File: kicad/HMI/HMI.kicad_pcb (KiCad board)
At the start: 2 copper layers, 47 x 107.1 mm, 57 parts, among them J2 SWD, J3 DEM 128128A TMH-PW-N, J4 RIBBON, SW1 SW_Push, SW10 SW_Push, SW11 SW_Push, SW12 SW_Push, SW13 SW_Push, SW14 SW_Push, SW15 SW_Push, SW16 SW_Push, SW17 SW_Push, SW18 SW_Push, SW19 SW_Push, SW2 SW_Push, SW20 SW_Push, SW3 SW_Push, SW4 SW_Push, SW5 SW_Push, SW6 SW_Push, SW7 SW_Push, SW8 SW_Push, SW9 SW_Push, U1 STM32L011K4Tx, X1 ASV-4.000MHZ-EJ-T

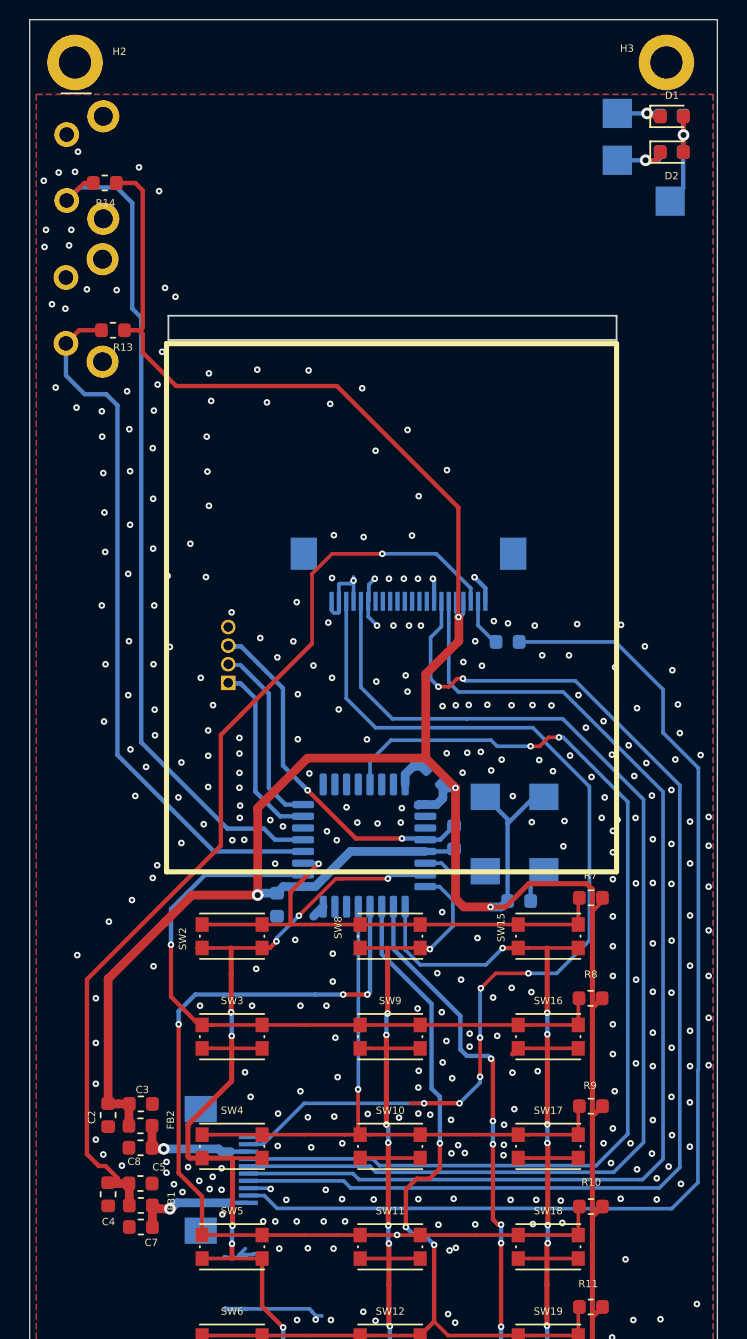
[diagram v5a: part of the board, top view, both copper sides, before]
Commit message: HMI: added labels on silksScreen -> added one capacitor -> generated new PDF -> generated new GERBERS -> NEW STEP!
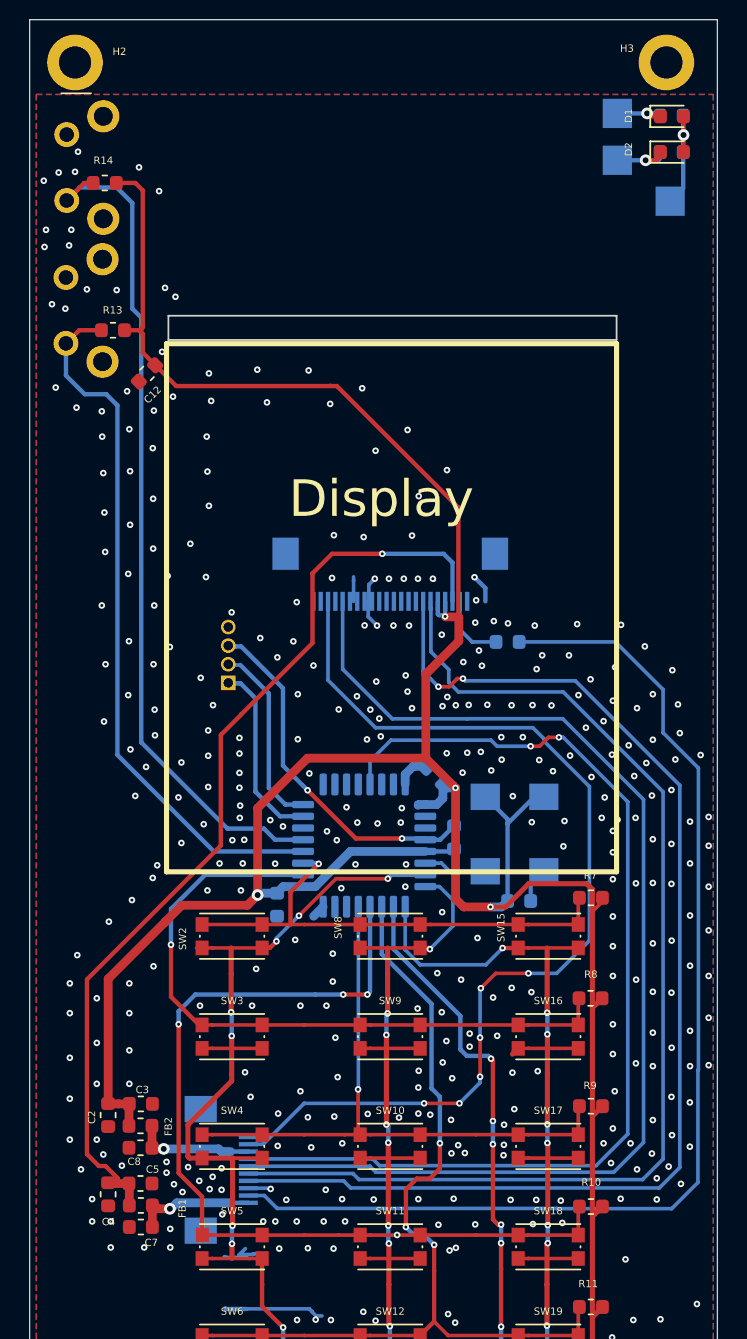
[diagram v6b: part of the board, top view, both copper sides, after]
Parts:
- added C12: 1u, Capacitor_SMD:C_0603_1608Metric, F.Cu at (126.7, 58.9)
- moved J3 1.24 mm to (143.3, 72.6)
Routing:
- net GND: track 31.5 -> 25.8 mm, vias 386 -> 424
- net TFT_RST: track 72.6 -> 69.7 mm
- net Net-(J3-Pad21): track 3.34 -> 4.85 mm
- net +3V3: track 196.2 -> 197.2 mm
- net SPI1_SCK: track 77.4 -> 77.9 mm
- net SPI1_MOSI: track 79.8 -> 80.3 mm
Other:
- board text added: "22"
- board text added: "Display"
- board text added: "Display interface"
- board text added: "FPC tape"
- board text added: "Mainboard connector"
- board text added: "SWD Interface"
